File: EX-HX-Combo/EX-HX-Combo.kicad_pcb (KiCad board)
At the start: 2 copper layers, 150.2 x 124.5 mm, 46 parts, among them CN1 DB9 Male, J1 IDE_CONNECTOR, J200 Bus_Tandy_Plus_Through, J3 Bus_Tandy_Plus, SW1 SW_DIP_x10, U1 BIOS FLASH, U2 74HCT245, U3 1.8432 MHz, U4 DS1315, U5 AS6C4008-55PCN, U6 16550/16C550, U7 GD75232N, U8 GAL16V8, U9 GAL16V8, Y1 32.768 KHz

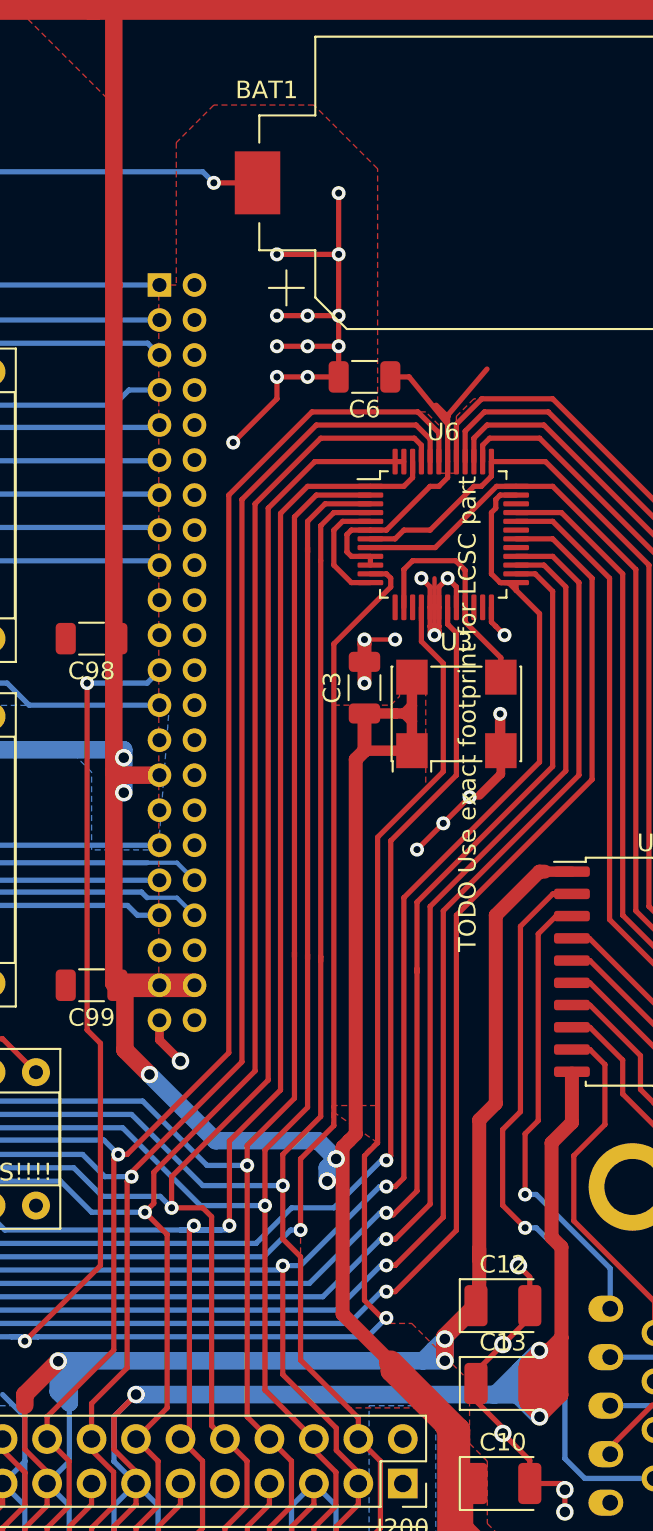
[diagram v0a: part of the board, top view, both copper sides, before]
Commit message: EX-HX-Combo: A little bit of power work for the CF connector.
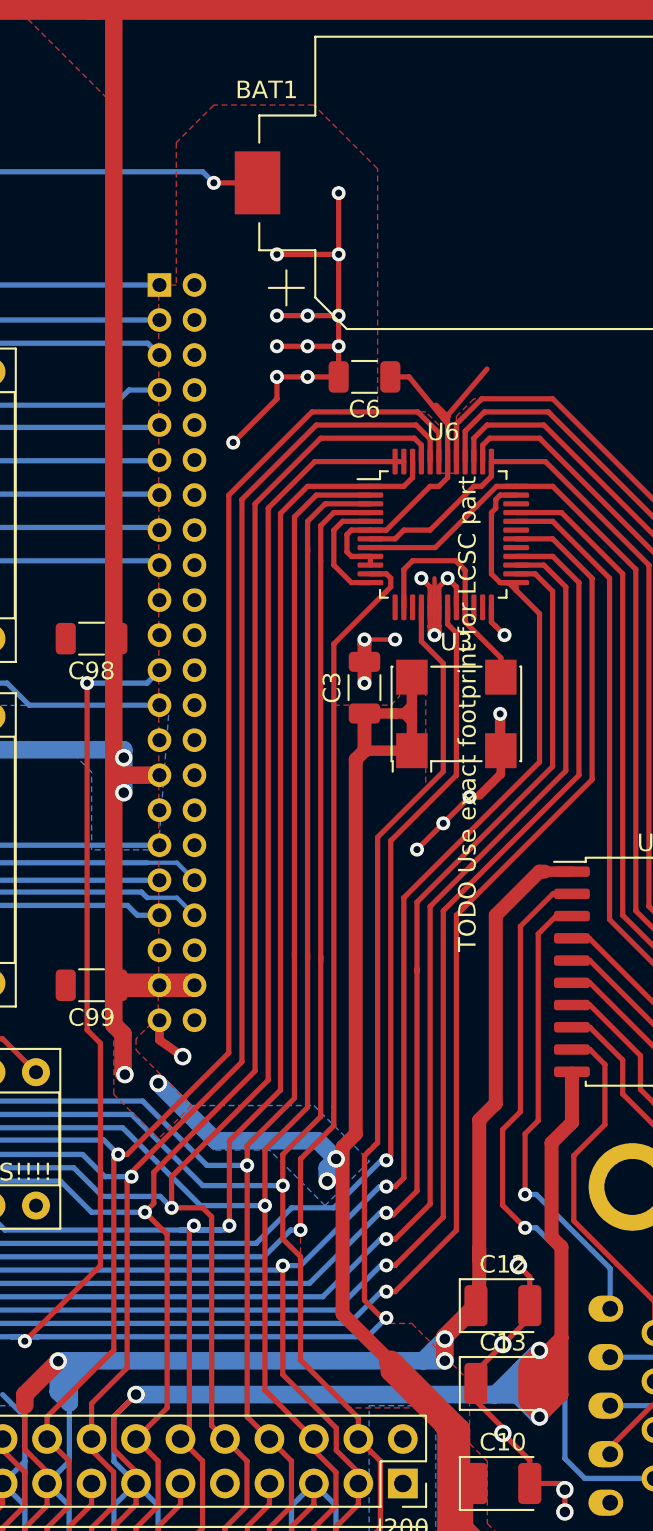
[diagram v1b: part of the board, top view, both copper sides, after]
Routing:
- net -12V: track 100.4 -> 108.1 mm
- net VCC: track 1307.0 -> 1306.0 mm, vias 14 -> 15

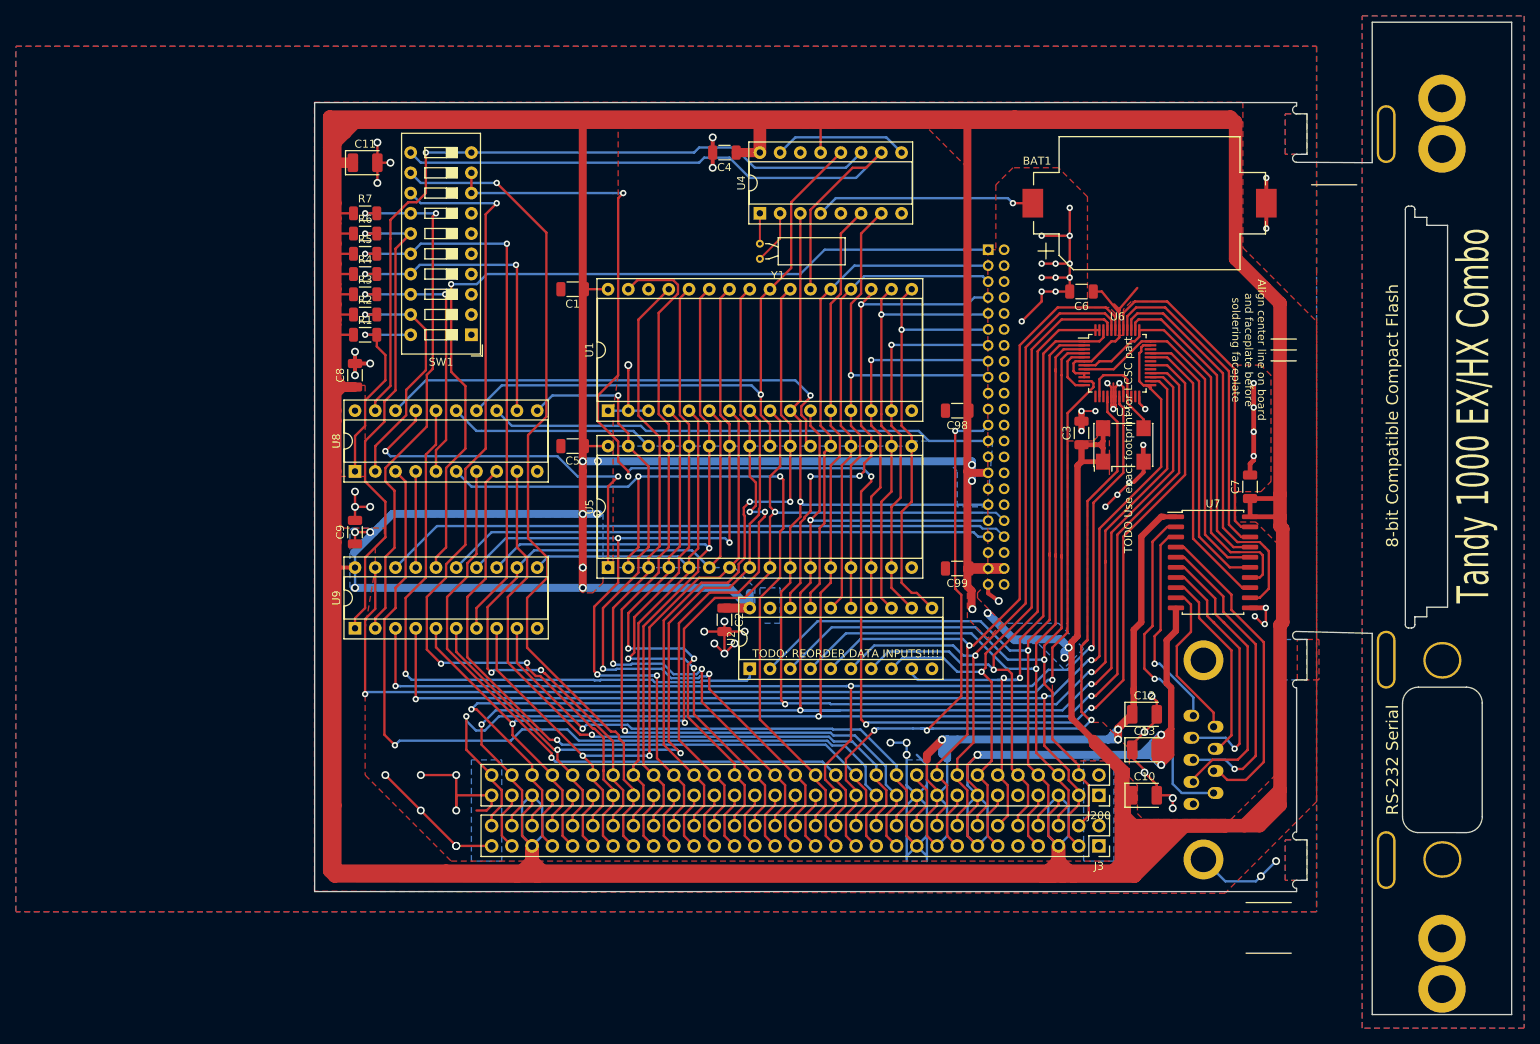
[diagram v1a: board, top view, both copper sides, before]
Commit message: Reorder dip switches on EX-HX-Combo.
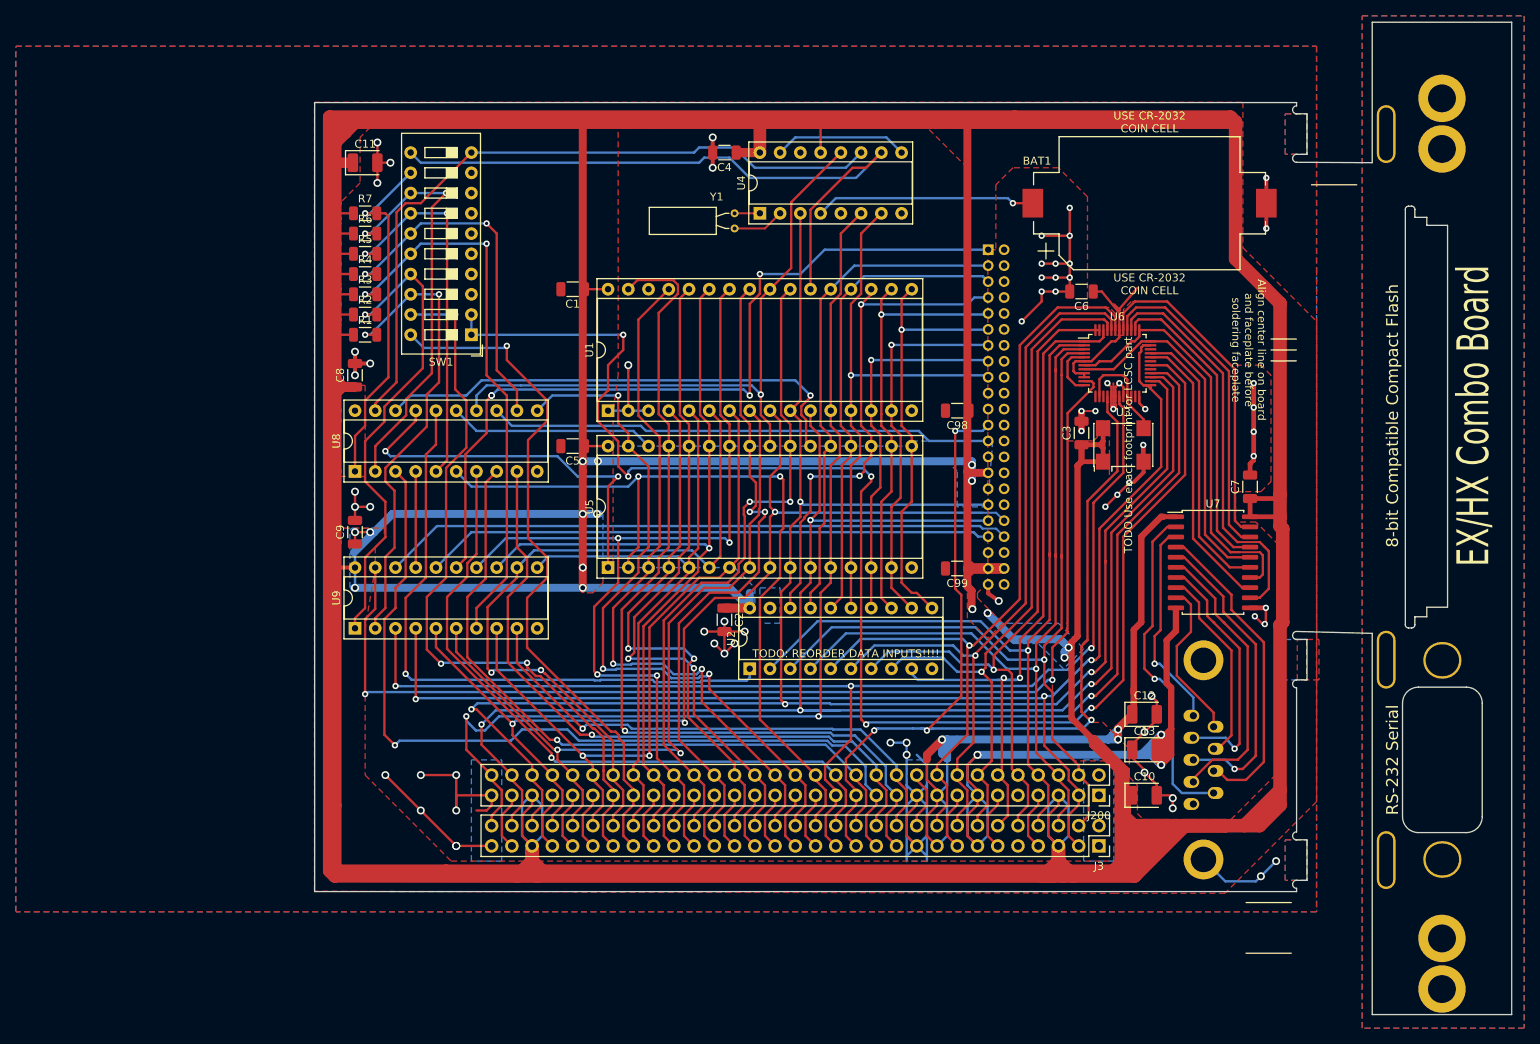
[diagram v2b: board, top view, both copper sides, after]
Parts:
- moved Y1 6.54 mm to (172.7, 51.4), turned to 270 degrees
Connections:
- R1 pad 2: BASE_RAM_ENABLE -> UART_S1
- R2 pad 2: BASE_RAM_SIZE -> UART_S0
- R3 pad 2: UMB_ENABLE -> ATA_ADDR_JUMPER
- R5 pad 2: ATA_ADDR_JUMPER -> UMB_ENABLE
- R6 pad 2: UART_S0 -> BASE_RAM_SIZE
- R7 pad 2: UART_S1 -> BASE_RAM_ENABLE
- SW1 pad 1: GND -> UART_IRQ
- SW1 pad 12: IRQ4 -> BASE_RAM_ENABLE
- SW1 pad 13: IRQ3 -> BASE_RAM_SIZE
- SW1 pad 14: UART_S1 -> UMB_ENABLE
- SW1 pad 15: UART_S0 -> UMB_SIZE
- SW1 pad 17: UMB_SIZE -> UART_S0
- SW1 pad 18: UMB_ENABLE -> UART_S1
- SW1 pad 19: BASE_RAM_SIZE -> IRQ3
- SW1 pad 2: GND -> UART_IRQ
- SW1 pad 20: BASE_RAM_ENABLE -> IRQ4
- SW1 pad 8: UART_IRQ -> GND
- SW1 pad 9: UART_IRQ -> GND
- U9 pad 15: ~CS1~_ATA -> ~RESET
- U9 pad 16: ~RESET -> ~CS1~_ATA
- Y1 pad 1: /RTC_X2 -> /RTC_X1
- Y1 pad 2: /RTC_X1 -> /RTC_X2
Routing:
- net BASE_RAM_SIZE: track 30.3 -> 52.3 mm, vias 1 -> 2
- net IRQ3: track 113.3 -> 92.6 mm
- net IRQ4: track 107.0 -> 87.8 mm
- net BASE_RAM_ENABLE: track 26.3 -> 44.6 mm
- net UART_IRQ: track 204.0 -> 186.2 mm
- net UMB_ENABLE: track 34.3 -> 46.8 mm
- net UART_S1: track 66.5 -> 59.0 mm
- net UMB_SIZE: track 39.2 -> 44.4 mm
- net ~RESET: track 107.0 -> 102.1 mm, vias 1 -> 4
- net ~CE~_BIOS_DECODE: track 92.4 -> 89.5 mm, vias 1 -> 0
- net ~CS1~_ATA: track 68.8 -> 71.4 mm
- net UART_S0: track 61.7 -> 60.0 mm
- net ~MEMR~_DELAYED: track 78.9 -> 80.1 mm
- net /RTC_X1: track 3.81 -> 3.18 mm
- net ATA_ADDR_JUMPER: track 69.6 -> 70.2 mm
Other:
- board text added: "EX/HX Combo Board"
- board text added: "USE CR-2032 COIN CELL"
- board text removed: "Tandy 1000 EX/HX Combo"

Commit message: Silkscreen work on EX-HX-Combo.
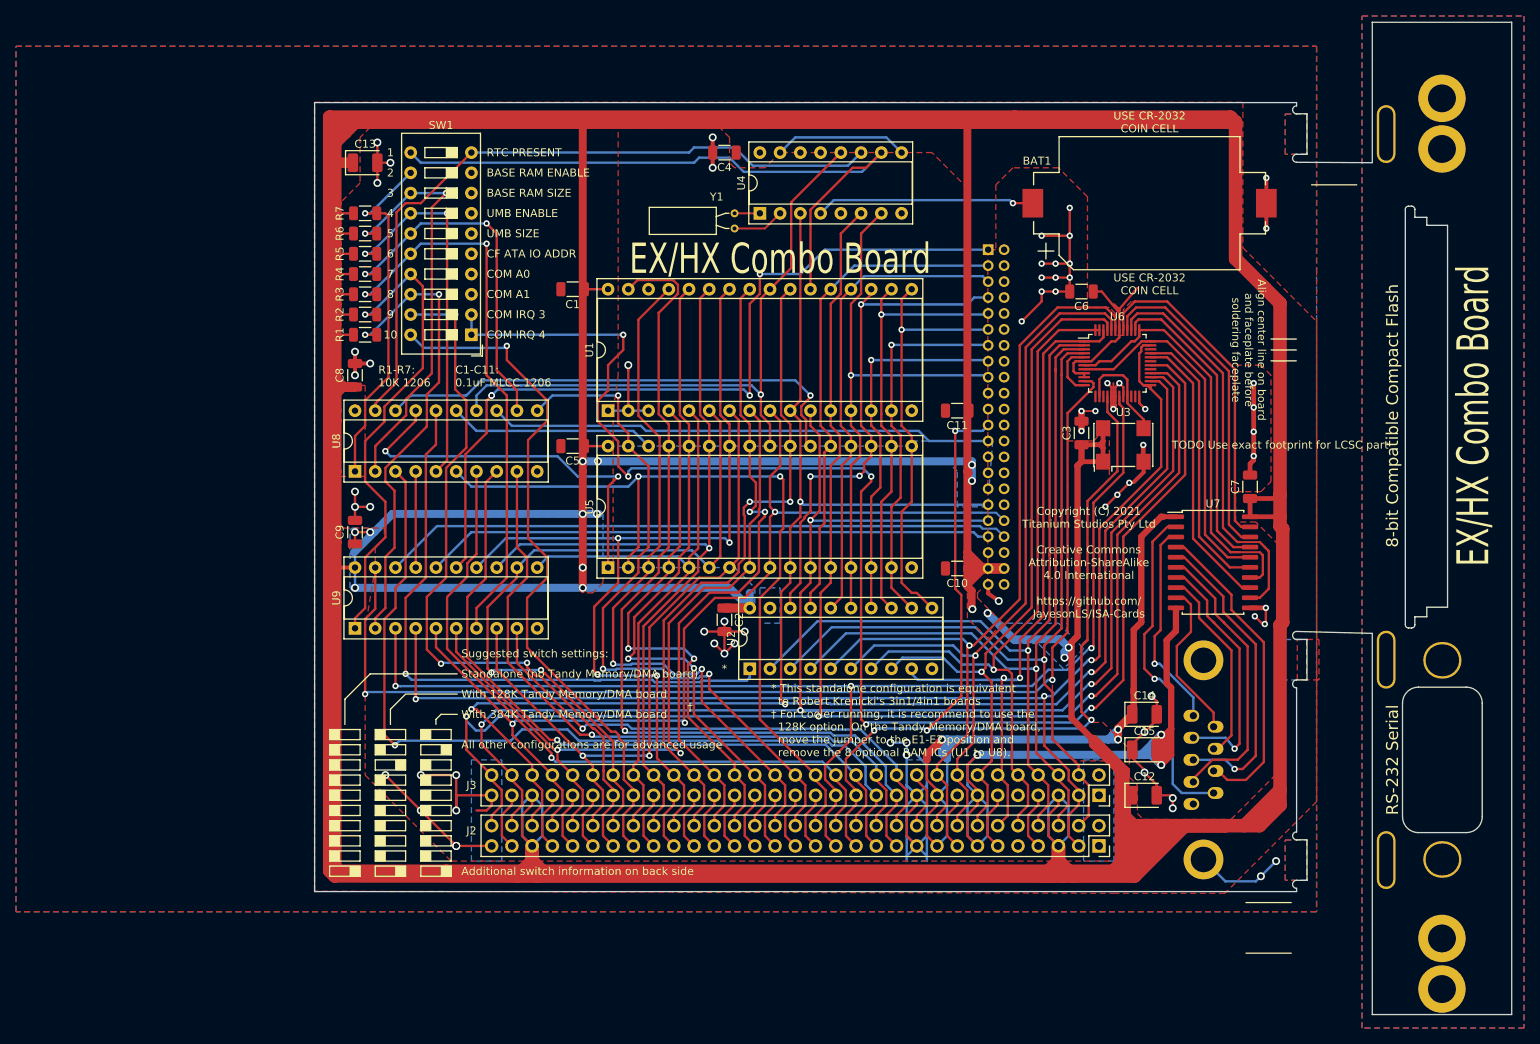
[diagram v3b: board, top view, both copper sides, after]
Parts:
- renumbered C99 to C10, C98 to C11, C10 to C12, C11 to C13, C12 to C14, C13 to C15, J3 to J2, J200 to J3
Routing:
- net VCC: track 1306.0 -> 1300.1 mm
- net ~CE~_BIOS_THRU: track 84.0 -> 83.4 mm
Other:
- board text added: "*"
- board text added: "* The 128k-160k UMB option is only for use on the Tandy 1000 EX. When the base RAM size is 384k, the UMB size will be 128k. Otherwise it will be 160k."
- board text added: "* This standalone configuration is equivalent to Robert Krenicki's 3in1/4in1 boards † For cooler running, it is recommend to use the 128K option. On the Tandy Memory/DMA board, move the jumper to the E1-E2 position and remove the 8 optional RAM ICs (U1 to U8)."
- board text added: "+256k"
- board text added: "+384k"
- board text added: "1"
- board text added: "10"
- board text added: "128k-160k"
- board text added: "1F0"
- board text added: "2"
- board text added: "3"
- board text added: "320"
- board text added: "4"
- board text added: "5"
- board text added: "6"
- board text added: "7"
- board text added: "8"
- board text added: "9"
- board text added: "96K"
- board text added: "Absent"
- board text added: "Additional switch information on back side"
- board text added: "All other configurations are for advanced usage"
- board text added: "BASE RAM ENABLE"
- board text added: "BASE RAM SIZE"
- board text added: "Base RAM"
- board text added: "Base RAM Size"
- board text added: "C1-C11: 0.1uF MLCC 1206"
- board text added: "CF ATA Address"
- board text added: "CF ATA IO ADDR"
- board text added: "COM A0"
- board text added: "COM A1"
- board text added: "COM IRQ"
- board text added: "COM IRQ 3"
- board text added: "COM IRQ 4"
- board text added: "COM/Serial Port"
- board text added: "COM1"
- board text added: "COM2"
- board text added: "COM3"
- board text added: "Copyright (C) 2021 Titanium Studios Pty Ltd Creative Commons Attribution-ShareAlike 4.0 International https://github.com/ JayesonLS/ISA-Cards"
- board text added: "DIP Switches 1 to 6:"
- board text added: "DIP Switches 7 to 10:"
- board text added: "Disabled"
- board text added: "Enabled"
- board text added: "IRQ3"
- board text added: "IRQ4"
- board text added: "Invalid"
- board text added: "None"
- board text added: "Present"
- board text added: "R1-R7: 10K 1206"
- board text added: "RTC PRESENT"
- board text added: "Real Time Clock"
- board text added: "Standalone (no Tandy Memory/DMA board)"
- board text added: "Suggested switch settings:"
- board text added: "Thanks to the XTIDE Universal BIOS Team and others who contributed to the XTIDE Universal BIOS. Additional thanks to Rob Krenicki, Jacob Dorne/Monotech PCs and James Pearce/Lo-tech for their influencing works."
- board text added: "UMB ENABLE"
- board text added: "UMB SIZE"
- board text added: "Upper Memory (UMB)"
- board text added: "Upper Memory Size*"
- board text added: "With 128K Tandy Memory/DMA board"
- board text added: "With 384K Tandy Memory/DMA board"
- board text added: "disabled or absent"
- board text added: "†"
- board text removed: "TODO: REORDER DATA INPUTS!!!!"
